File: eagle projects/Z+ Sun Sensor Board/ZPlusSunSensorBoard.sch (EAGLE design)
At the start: 51 parts, among them J1 Power In, J2 Power Out, U1 TSV991AILT, U2 ADS7841E_2K5, U4 LM20BIM7X_NOPB, U5 TSV991AILT, U8 TSV991AILT

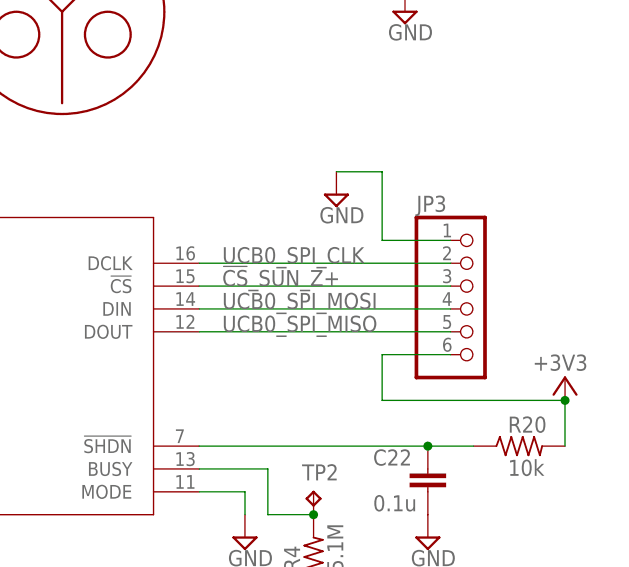
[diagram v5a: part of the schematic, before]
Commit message: Solder Cups on Z+ Board
Replace previous connector on Z+ Sun Sensor Board with solder cups. Rearranged wires to fit the new component.
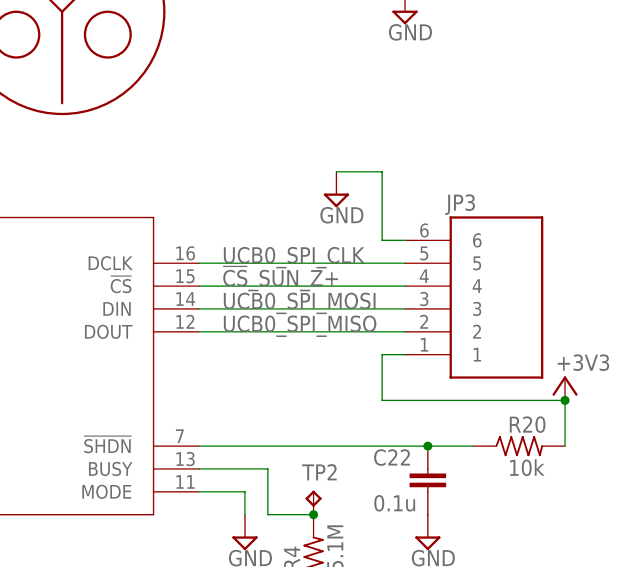
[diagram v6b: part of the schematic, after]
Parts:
- JP3: value (none) -> 830-10-006-20-005000; device my_library:PINHD-1X6 -> 830-10-006-20-005000:830-10-006-20-005000
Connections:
- net !CS!_SUN_Z+: now also JP3.4; no longer JP3.3
- net +3V3: now also JP3.1; no longer JP3.6
- net GND: now also JP3.6; no longer JP3.1
- net UCB0_SPI_CLK: now also JP3.5; no longer JP3.2
- net UCB0_SPI_MISO: now also JP3.2; no longer JP3.5
- net UCB0_SPI_MOSI: now also JP3.3; no longer JP3.4
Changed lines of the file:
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@@
 <drawing>
 <settings>
-<setting alwaysvectorfont="yes"/>
+<setting alwaysvectorfont="no"/>
 <setting verticaltext="up"/>
 </settings>
@@
 <part name="R2" library="rcl" library_urn="urn:adsk.eagle:library:334" deviceset="R-US_" device="R0805" package3d_urn="urn:adsk.eagle:package:23553/2" value="0R"/>
 <part name="TP2" library="my_library" library_urn="urn:adsk.eagle:library:22876504" deviceset="TESTPOINT" device="" package3d_urn="urn:adsk.eagle:package:24605432/3"/>
-<part name="JP3" library="my_library" library_urn="urn:adsk.eagle:library:22876504" deviceset="PINHD-1X6" device="" package3d_urn="urn:adsk.eagle:package:26872615/1"/>
 <part name="SUPPLY1" library="supply2" library_urn="urn:adsk.eagle:library:372" deviceset="GND" device=""/>
 <part name="SUPPLY2" library="supply2" library_urn="urn:adsk.eagle:library:372" deviceset="GND" device=""/>
@@
 <part name="J1" library="PDUv1" library_urn="urn:adsk.eagle:library:29653418" deviceset="2038638103" device="" package3d_urn="urn:adsk.eagle:package:30104253/5" value="Power In"/>
 <part name="J2" library="PDUv1" library_urn="urn:adsk.eagle:library:29653418" deviceset="2038638103" device="" package3d_urn="urn:adsk.eagle:package:30104253/5" value="Power Out"/>
+<part name="JP3" library="830-10-006-20-005000" deviceset="830-10-006-20-005000" device=""/>
 </parts>
 <sheets>
@@
 </instance>
 <instance part="+3V18" gate="G$1" x="261.62" y="114.3" smashed="yes">
-<attribute name="VALUE" x="264.16" y="116.84" size="1.778" layer="96" rot="R180"/>
+<attribute name="VALUE" x="266.7" y="116.84" size="1.778" layer="96" rot="R180"/>
 </instance>
 <instance part="R20" gate="G$1" x="256.54" y="106.68" smashed="yes">
@@
 <instance part="TP2" gate="G$1" x="233.68" y="101.6" smashed="yes">
 <attribute name="NAME" x="232.41" y="102.87" size="1.778" layer="95"/>
-</instance>
-<instance part="JP3" gate="A" x="251.46" y="121.92" smashed="yes">
-<attribute name="NAME" x="245.11" y="132.715" size="1.778" layer="95"/>
-<attribute name="VALUE" x="245.11" y="111.76" size="1.778" layer="96"/>
 </instance>
 <instance part="SUPPLY1" gate="GND" x="236.22" y="134.62" smashed="yes">
@@
 <attribute name="VALUE" x="238.76" y="182.88" size="1.778" layer="96"/>
 </instance>
+<instance part="JP3" gate="G$1" x="254" y="121.92" smashed="yes" rot="MR180">
+<attribute name="NAME" x="248.42" y="134.62" size="1.778" layer="95" rot="MR180"/>
+</instance>
 </instances>
 <busses>
@@
 <net name="UCB0_SPI_MOSI" class="0">
 <segment>
-<wire x1="248.92" y1="121.92" x2="220.98" y2="121.92" width="0.1524" layer="91"/>
+<wire x1="243.84" y1="121.92" x2="220.98" y2="121.92" width="0.1524" layer="91"/>
 <label x="223.52" y="121.92" size="1.778" layer="95"/>
 <pinref part="U2" gate="A" pin="DIN"/>
-<pinref part="JP3" gate="A" pin="4"/>
+<pinref part="JP3" gate="G$1" pin="3"/>
 </segment>
 </net>
 <net name="UCB0_SPI_CLK" class="0">
 <segment>
-<wire x1="248.92" y1="127" x2="220.98" y2="127" width="0.1524" layer="91"/>
+<wire x1="243.84" y1="127" x2="220.98" y2="127" width="0.1524" layer="91"/>
 <label x="223.52" y="127" size="1.778" layer="95"/>
 <pinref part="U2" gate="A" pin="DCLK"/>
-<pinref part="JP3" gate="A" pin="2"/>
+<pinref part="JP3" gate="G$1" pin="5"/>
 </segment>
 </net>
 <net name="UCB0_SPI_MISO" class="0">
 <segment>
-<wire x1="248.92" y1="119.38" x2="220.98" y2="119.38" width="0.1524" layer="91"/>
+<wire x1="243.84" y1="119.38" x2="220.98" y2="119.38" width="0.1524" layer="91"/>
 <label x="223.52" y="119.38" size="1.778" layer="95"/>
 <pinref part="U2" gate="A" pin="DOUT"/>
-<pinref part="JP3" gate="A" pin="5"/>
+<pinref part="JP3" gate="G$1" pin="2"/>
 </segment>
 </net>
 <net name="!CS!_SUN_Z+" class="0">
 <segment>
-<wire x1="248.92" y1="124.46" x2="220.98" y2="124.46" width="0.1524" layer="91"/>
+<wire x1="243.84" y1="124.46" x2="220.98" y2="124.46" width="0.1524" layer="91"/>
 <label x="223.52" y="124.46" size="1.778" layer="95"/>
 <pinref part="U2" gate="A" pin="!CS"/>
-<pinref part="JP3" gate="A" pin="3"/>
+<pinref part="JP3" gate="G$1" pin="4"/>
 </segment>
 </net>
@@
 <wire x1="261.62" y1="106.68" x2="261.62" y2="111.76" width="0.1524" layer="91"/>
 <pinref part="R20" gate="G$1" pin="2"/>
-<pinref part="JP3" gate="A" pin="6"/>
-<wire x1="248.92" y1="116.84" x2="241.3" y2="116.84" width="0.1524" layer="91"/>
+<wire x1="243.84" y1="116.84" x2="241.3" y2="116.84" width="0.1524" layer="91"/>
 <wire x1="241.3" y1="116.84" x2="241.3" y2="111.76" width="0.1524" layer="91"/>
 <wire x1="241.3" y1="111.76" x2="261.62" y2="111.76" width="0.1524" layer="91"/>
 <junction x="261.62" y="111.76"/>
+<pinref part="JP3" gate="G$1" pin="1"/>
 </segment>
 <segment>
@@
 </segment>
 <segment>
-<pinref part="JP3" gate="A" pin="1"/>
-<wire x1="248.92" y1="129.54" x2="241.3" y2="129.54" width="0.1524" layer="91"/>
+<wire x1="243.84" y1="129.54" x2="241.3" y2="129.54" width="0.1524" layer="91"/>
 <wire x1="241.3" y1="129.54" x2="241.3" y2="137.16" width="0.1524" layer="91"/>
 <wire x1="241.3" y1="137.16" x2="236.22" y2="137.16" width="0.1524" layer="91"/>
 <pinref part="SUPPLY1" gate="GND" pin="GND"/>
-</segment>
-<segment>
+<pinref part="JP3" gate="G$1" pin="6"/>
+</segment>
+<segment>

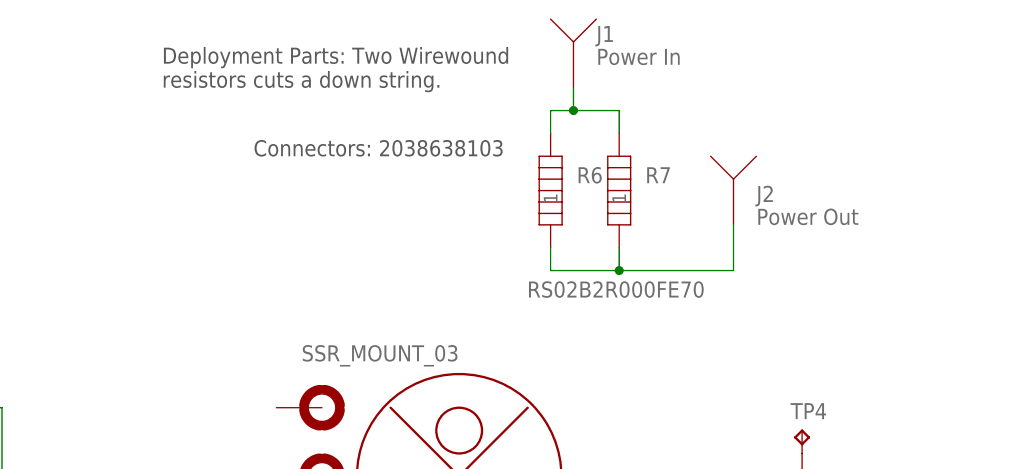
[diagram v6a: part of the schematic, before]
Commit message: Added Luc's recommended new power connectors
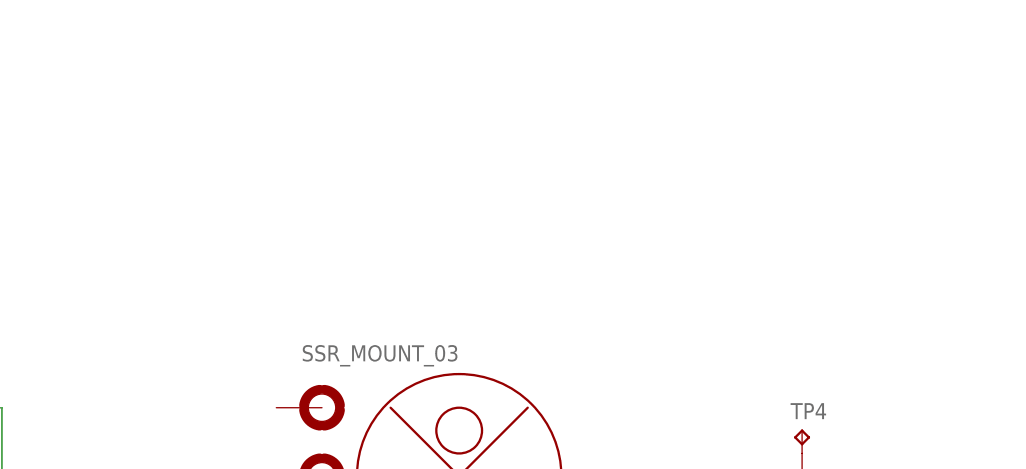
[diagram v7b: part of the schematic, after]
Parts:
- removed J1: Power In, PDUv1:2038638103
- removed J2: Power Out, PDUv1:2038638103
- removed R6, R7: RS02B2R000FE70, Heating Element:RS02B2R000FE70
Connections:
- removed net N$5: J1.P$1, R6.2, R7.2
- removed net N$6: J2.P$1, R6.1, R7.1
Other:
- note removed: "Connectors: 2038638103"
- note removed: "Deployment Parts: Two Wirewound resistors cuts a down string."
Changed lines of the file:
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@@
 <part name="SUPPLY15" library="supply2" library_urn="urn:adsk.eagle:library:372" deviceset="GND" device=""/>
 <part name="SUPPLY16" library="supply2" library_urn="urn:adsk.eagle:library:372" deviceset="GND" device=""/>
-<part name="R6" library="Heating Element" library_urn="urn:adsk.eagle:library:29300905" deviceset="RS02B2R000FE70" device="" package3d_urn="urn:adsk.eagle:package:29301001/2"/>
-<part name="R7" library="Heating Element" library_urn="urn:adsk.eagle:library:29300905" deviceset="RS02B2R000FE70" device="" package3d_urn="urn:adsk.eagle:package:29301001/2"/>
-<part name="J1" library="PDUv1" library_urn="urn:adsk.eagle:library:29653418" deviceset="2038638103" device="" package3d_urn="urn:adsk.eagle:package:30104253/5" value="Power In"/>
-<part name="J2" library="PDUv1" library_urn="urn:adsk.eagle:library:29653418" deviceset="2038638103" device="" package3d_urn="urn:adsk.eagle:package:30104253/5" value="Power Out"/>
 <part name="JP3" library="830-10-006-20-005000" deviceset="830-10-006-20-005000" device=""/>
 </parts>
@@
 <text x="262.128" y="7.112" size="2.54" layer="94">B</text>
 <text x="190.754" y="11.43" size="2.54" layer="94">T. Christison</text>
-<text x="182.88" y="190.5" size="1.778" layer="97">Connectors: 2038638103</text>
-<text x="172.72" y="198.12" size="1.778" layer="97">Deployment Parts: Two Wirewound
-resistors cuts a down string.</text>
 </plain>
 <instances>
@@
 <instance part="SUPPLY16" gate="GND" x="129.54" y="7.62" smashed="yes">
 <attribute name="VALUE" x="127.635" y="4.445" size="1.778" layer="96"/>
-</instance>
-<instance part="R6" gate="A" x="215.9" y="180.34" smashed="yes" rot="R90">
-<attribute name="VALUE" x="213.2838" y="174.8028" size="1.778" layer="96" ratio="10" rot="SR0"/>
-<attribute name="NAME" x="218.7956" y="187.5028" size="1.778" layer="95" ratio="10" rot="SR0"/>
-</instance>
-<instance part="R7" gate="A" x="223.52" y="180.34" smashed="yes" rot="R90">
-<attribute name="NAME" x="226.4156" y="187.5028" size="1.778" layer="95" ratio="10" rot="SR0"/>
-</instance>
-<instance part="J1" gate="G$1" x="218.44" y="203.2" smashed="yes" rot="R90">
-<attribute name="NAME" x="220.98" y="203.2" size="1.778" layer="95"/>
-<attribute name="VALUE" x="220.98" y="200.66" size="1.778" layer="96"/>
-</instance>
-<instance part="J2" gate="G$1" x="236.22" y="187.96" smashed="yes" rot="R90">
-<attribute name="NAME" x="238.76" y="185.42" size="1.778" layer="95"/>
-<attribute name="VALUE" x="238.76" y="182.88" size="1.778" layer="96"/>
 </instance>
 <instance part="JP3" gate="G$1" x="254" y="121.92" smashed="yes" rot="MR180">
@@
 </segment>
 </net>
-<net name="N$5" class="0">
-<segment>
-<pinref part="R6" gate="A" pin="2"/>
-<wire x1="215.9" y1="193.04" x2="215.9" y2="195.58" width="0.1524" layer="91"/>
-<wire x1="215.9" y1="195.58" x2="218.44" y2="195.58" width="0.1524" layer="91"/>
-<pinref part="R7" gate="A" pin="2"/>
-<wire x1="218.44" y1="195.58" x2="223.52" y2="195.58" width="0.1524" layer="91"/>
-<wire x1="223.52" y1="195.58" x2="223.52" y2="193.04" width="0.1524" layer="91"/>
-<wire x1="218.44" y1="198.12" x2="218.44" y2="195.58" width="0.1524" layer="91"/>
-<junction x="218.44" y="195.58"/>
-<pinref part="J1" gate="G$1" pin="P$1"/>
-</segment>
-</net>
-<net name="N$6" class="0">
-<segment>
-<pinref part="R6" gate="A" pin="1"/>
-<wire x1="215.9" y1="180.34" x2="215.9" y2="177.8" width="0.1524" layer="91"/>
-<pinref part="R7" gate="A" pin="1"/>
-<wire x1="215.9" y1="177.8" x2="223.52" y2="177.8" width="0.1524" layer="91"/>
-<wire x1="223.52" y1="177.8" x2="223.52" y2="180.34" width="0.1524" layer="91"/>
-<wire x1="236.22" y1="177.8" x2="223.52" y2="177.8" width="0.1524" layer="91"/>
-<junction x="223.52" y="177.8"/>
-<wire x1="236.22" y1="182.88" x2="236.22" y2="177.8" width="0.1524" layer="91"/>
-<pinref part="J2" gate="G$1" pin="P$1"/>
-</segment>
-</net>
 </nets>
 </sheet>
@@
 </drawing>
 <compatibility>
-<note version="6.3" minversion="6.2.2" severity="warning">
-Since Version 6.2.2 text objects can contain more than one line,
-which will not be processed correctly with this version.
-</note>
 <note version="8.2" severity="warning">
 Since Version 8.2, EAGLE supports online libraries. The ids

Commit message: Revert "Added Luc's recommended new power connectors"
This reverts commit dfe48c56fe37fa57a9af7eb032061edffce3900f.
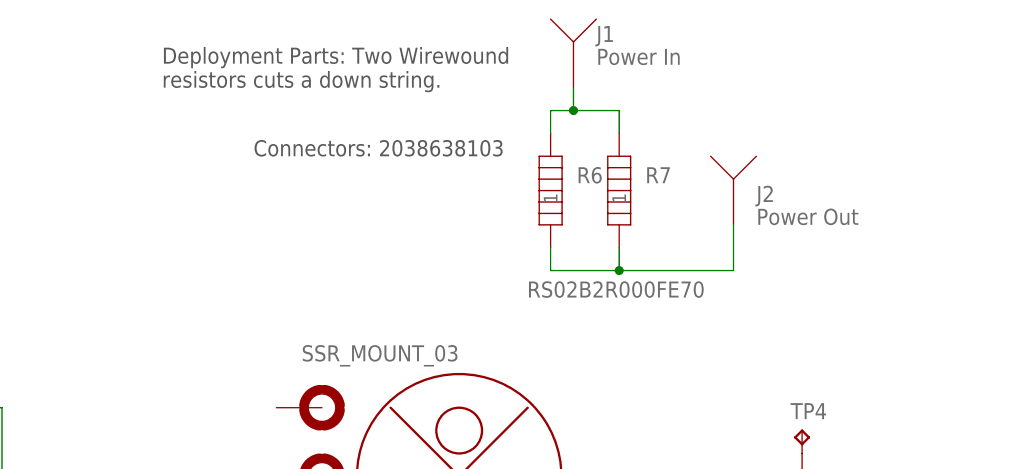
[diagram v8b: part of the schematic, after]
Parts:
- added J1: Power In, PDUv1:2038638103
- added J2: Power Out, PDUv1:2038638103
- added R6, R7: RS02B2R000FE70, Heating Element:RS02B2R000FE70
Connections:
- new net N$5: J1.P$1, R6.2, R7.2
- new net N$6: J2.P$1, R6.1, R7.1
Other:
- note added: "Connectors: 2038638103"
- note added: "Deployment Parts: Two Wirewound resistors cuts a down string."
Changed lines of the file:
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@@
 <part name="SUPPLY15" library="supply2" library_urn="urn:adsk.eagle:library:372" deviceset="GND" device=""/>
 <part name="SUPPLY16" library="supply2" library_urn="urn:adsk.eagle:library:372" deviceset="GND" device=""/>
+<part name="R6" library="Heating Element" library_urn="urn:adsk.eagle:library:29300905" deviceset="RS02B2R000FE70" device="" package3d_urn="urn:adsk.eagle:package:29301001/2"/>
+<part name="R7" library="Heating Element" library_urn="urn:adsk.eagle:library:29300905" deviceset="RS02B2R000FE70" device="" package3d_urn="urn:adsk.eagle:package:29301001/2"/>
+<part name="J1" library="PDUv1" library_urn="urn:adsk.eagle:library:29653418" deviceset="2038638103" device="" package3d_urn="urn:adsk.eagle:package:30104253/5" value="Power In"/>
+<part name="J2" library="PDUv1" library_urn="urn:adsk.eagle:library:29653418" deviceset="2038638103" device="" package3d_urn="urn:adsk.eagle:package:30104253/5" value="Power Out"/>
 <part name="JP3" library="830-10-006-20-005000" deviceset="830-10-006-20-005000" device=""/>
 </parts>
@@
 <text x="262.128" y="7.112" size="2.54" layer="94">B</text>
 <text x="190.754" y="11.43" size="2.54" layer="94">T. Christison</text>
+<text x="182.88" y="190.5" size="1.778" layer="97">Connectors: 2038638103</text>
+<text x="172.72" y="198.12" size="1.778" layer="97">Deployment Parts: Two Wirewound
+resistors cuts a down string.</text>
 </plain>
 <instances>
@@
 <instance part="SUPPLY16" gate="GND" x="129.54" y="7.62" smashed="yes">
 <attribute name="VALUE" x="127.635" y="4.445" size="1.778" layer="96"/>
+</instance>
+<instance part="R6" gate="A" x="215.9" y="180.34" smashed="yes" rot="R90">
+<attribute name="VALUE" x="213.2838" y="174.8028" size="1.778" layer="96" ratio="10" rot="SR0"/>
+<attribute name="NAME" x="218.7956" y="187.5028" size="1.778" layer="95" ratio="10" rot="SR0"/>
+</instance>
+<instance part="R7" gate="A" x="223.52" y="180.34" smashed="yes" rot="R90">
+<attribute name="NAME" x="226.4156" y="187.5028" size="1.778" layer="95" ratio="10" rot="SR0"/>
+</instance>
+<instance part="J1" gate="G$1" x="218.44" y="203.2" smashed="yes" rot="R90">
+<attribute name="NAME" x="220.98" y="203.2" size="1.778" layer="95"/>
+<attribute name="VALUE" x="220.98" y="200.66" size="1.778" layer="96"/>
+</instance>
+<instance part="J2" gate="G$1" x="236.22" y="187.96" smashed="yes" rot="R90">
+<attribute name="NAME" x="238.76" y="185.42" size="1.778" layer="95"/>
+<attribute name="VALUE" x="238.76" y="182.88" size="1.778" layer="96"/>
 </instance>
 <instance part="JP3" gate="G$1" x="254" y="121.92" smashed="yes" rot="MR180">
@@
 </segment>
 </net>
+<net name="N$5" class="0">
+<segment>
+<pinref part="R6" gate="A" pin="2"/>
+<wire x1="215.9" y1="193.04" x2="215.9" y2="195.58" width="0.1524" layer="91"/>
+<wire x1="215.9" y1="195.58" x2="218.44" y2="195.58" width="0.1524" layer="91"/>
+<pinref part="R7" gate="A" pin="2"/>
+<wire x1="218.44" y1="195.58" x2="223.52" y2="195.58" width="0.1524" layer="91"/>
+<wire x1="223.52" y1="195.58" x2="223.52" y2="193.04" width="0.1524" layer="91"/>
+<wire x1="218.44" y1="198.12" x2="218.44" y2="195.58" width="0.1524" layer="91"/>
+<junction x="218.44" y="195.58"/>
+<pinref part="J1" gate="G$1" pin="P$1"/>
+</segment>
+</net>
+<net name="N$6" class="0">
+<segment>
+<pinref part="R6" gate="A" pin="1"/>
+<wire x1="215.9" y1="180.34" x2="215.9" y2="177.8" width="0.1524" layer="91"/>
+<pinref part="R7" gate="A" pin="1"/>
+<wire x1="215.9" y1="177.8" x2="223.52" y2="177.8" width="0.1524" layer="91"/>
+<wire x1="223.52" y1="177.8" x2="223.52" y2="180.34" width="0.1524" layer="91"/>
+<wire x1="236.22" y1="177.8" x2="223.52" y2="177.8" width="0.1524" layer="91"/>
+<junction x="223.52" y="177.8"/>
+<wire x1="236.22" y1="182.88" x2="236.22" y2="177.8" width="0.1524" layer="91"/>
+<pinref part="J2" gate="G$1" pin="P$1"/>
+</segment>
+</net>
 </nets>
 </sheet>
@@
 </drawing>
 <compatibility>
+<note version="6.3" minversion="6.2.2" severity="warning">
+Since Version 6.2.2 text objects can contain more than one line,
+which will not be processed correctly with this version.
+</note>
 <note version="8.2" severity="warning">
 Since Version 8.2, EAGLE supports online libraries. The ids
